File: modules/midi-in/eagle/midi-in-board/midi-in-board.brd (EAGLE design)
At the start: 100 x 80 mm, 83 parts, among them IC1 LM358N, IC2 TL072P, IC3 TL074P, IC4 TL074P, T1 BC547, T2 BC547, T3 BC547, X1 MIDI IN, X2 MIDI THRU, X3 CHANNEL SELECT SW, X4 POWER IN

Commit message: Start PCB design for main MIDI in board
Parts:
- removed C7: 100n, rcl:C050-024X044
- removed JP5, JP6: (no value), pinhead:1X02
- removed R52, R53: 220R, rcl:0207/7
- removed T3: BC547, transistor:TO92
- removed V1, V2: 74595N, 74ttl-din:DIL16
- JP1: device pinhead:1X08 -> pinhead:1_05X2MM
- JP2: device pinhead:1X08 -> pinhead:1X02
- JP3: device pinhead:1X01 -> pinhead:1X02
- R1: value 220R -> 1K
- R11: value 1K -> 10K
- R15, R49: value 10K -> 1K; device rcl:0207/7 -> pot:CA6V
- R18, R20, R24, R26, R27: value 10K -> 100K
- R2, R5, R50: value 10K -> 220R
- R28, R29, R30, R31, R32: value 100K -> 10K
- R34, R36, R38: value 3.6K -> 10K
- R4: value 220R -> 10K
- R41: value 10K -> 3.6K
- R43, R44: value 1K -> 3.6K; device pot:CA6V -> rcl:0207/7
- R48: value 20K -> 1K; device rcl:0207/7 -> pot:CA6V
- R51: value 1K -> 220R; device pot:CA6V -> rcl:0207/7
- R6: value 10K -> 20K
- X1: value MIDI IN -> POWER IN; device con-molex:22-23-2021 -> con-wago-500:W237-103
- X2: value MIDI THRU -> MIDI IN; device con-molex:22-23-2031 -> con-molex:22-23-2021
- X3: value CHANNEL SELECT SW -> MIDI THRU; device con-molex:22-23-2021 -> con-molex:22-23-2031
- X4: value POWER IN -> CHANNEL SELECT SW; device con-wago-500:W237-103 -> con-molex:22-23-2021
- moved R1 132.3 mm to (90.2, 55.9), turned to 90 degrees
- moved SV2 131.2 mm to (69.8, 54.6)
- moved X4 119.5 mm to (95.2, 53.3), turned to 90 degrees
- moved X1 116.6 mm to (52.1, 11.4)
- moved R4 106.7 mm to (33.0, 47.0), turned to 90 degrees
- moved SV1 101.4 mm to (69.8, 66.0)
- moved R51 100.6 mm to (-27.9, 95.2)
- moved R5 100.0 mm to (12.7, 33.0), turned to 270 degrees
- moved IC1 95.3 mm to (24.1, 31.8), turned to 90 degrees
- moved R44 86.0 mm to (-58.4, 90.2)
- moved R49 84.8 mm to (-66.0, 6.35)
- moved R48 84.6 mm to (-57.1, 6.35)
- moved R43 84.2 mm to (-38.1, 90.2)
- moved R15 83.1 mm to (-74.9, 6.35)
- moved R2 76.1 mm to (16.5, 30.5), turned to 270 degrees
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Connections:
- removed net +UB: V1.16, V2.16
- removed net -UB: V1.8, V2.8
- removed net N$1 (its old number): R1.1, X1.1
- removed net N$25: V1.9, V2.14
- removed net N$30: C2.2, R10.2, V1.10, V2.10
- removed net N$48: JP1.1, V1.15
- removed net N$49: JP1.2, V1.1
- removed net N$50: JP1.3, V1.2
- removed net N$51: JP1.4, V1.3
- removed net N$52: JP1.5, V1.4
- removed net N$54: JP1.6, V1.5
- removed net N$55: JP1.7, V1.6
- removed net N$58: JP1.8, V1.7
- removed net N$60: JP2.1, V2.15
- removed net N$64 (its old number): R38.2, R45.E
- removed net N$72: JP2.2, V2.1
- removed net N$73: JP2.3, V2.2
- removed net N$74: JP2.4, V2.3
- removed net N$75: JP2.5, V2.4
- removed net N$76: JP2.6, V2.5
- removed net N$77: JP2.7, V2.6
- removed net N$78: JP2.8, V2.7
- removed net N$8: R9.1, T3.2
- removed net V-: C1.1, C2.1, IC1.8, OK1.8, R11.2, R2.2, R3.2, R9.2, SV1.4, T1.3, T2.3, T3.3
- new net N$6: R2.1, X3.1
- new net N$66: R44.2, R49.E
- net GND: now also C2.2, JP1.1, JP2.2, JP3.2, R10.2, R11.2, R14.1, R16.1, R28.1, R8.2, R9.2, X1.2; no longer C7.2, JP5.2, JP6.2, R10.1, R13.2, R14.2, R15.2, R16.2, R50.1, R6.1, R8.1, T3.1, V1.13, V2.13, X2.2
- net N$10: now also R32.2, R33.2, R38.1; no longer R24.2, R26.2, R39.1
- net N$11: now also R7.1; no longer R5.1
- net N$12: now also R22.1; no longer R7.1
- net N$13: now also C2.1, R8.1; no longer C3.1, R12.1
- net N$14: now also R1.1, X4.1; no longer R11.1, X3.1
- net N$15: now also C3.1, R18.1, R9.1; no longer C4.1, R13.1, R19.1
- net N$16: now also C4.1, R10.1, R19.1; no longer C5.1, R14.1, R21.1
- net N$17: now also C5.1, R11.1, R20.1; no longer C6.1, R15.1, R23.1
- net N$18: now also C6.1, R12.1, R21.1; no longer C7.1, R16.1, R25.1
- net N$19: now also R7.2; no longer R5.2
- net N$2: now also R3.2; no longer R1.2
- net N$20: now also R16.2, R50.1; no longer R52.1, R6.2
- net N$21: now also R22.2; no longer R7.2
- net N$22: now also R28.2, R51.1; no longer R53.1, R8.2
- net N$23: now also R26.2, R32.1, R33.1; no longer R24.1, R26.1, R31.2
- net N$24: now also JP1.4; no longer V1.11, V2.11
- net N$26: now also JP1.3; no longer V1.12, V2.12
- net N$27: now also R23.1; no longer R28.1
- net N$28: now also R18.2, R24.1; no longer R19.2, R29.1
- net N$29: now also R19.2, R25.1; no longer R21.2, R30.1
- net N$3: now also X2.2; no longer X1.2
- net N$31: now also R20.2, R26.1; no longer R23.2, R31.1
- net N$32: now also R21.2, R27.1; no longer R25.2, R32.1
- net N$33: now also R23.2, R29.1; no longer R18.1, R28.2
- net N$34: now also R29.2, R35.1; no longer R18.2, R33.1
- net N$35: now also R24.2, R30.1; no longer R20.1, R29.2
- net N$36: now also R30.2, R36.1; no longer R20.2, R35.1
- net N$37: now also R25.2, R31.1; no longer R22.1, R30.2
- net N$38: now also R31.2; no longer R22.2
- net N$39: now also R27.2, R34.1; no longer R27.1, R32.2
- net N$4: now also R5.1; no longer R4.1
- net N$40: now also R34.2, R39.1; no longer R27.2, R41.1
- net N$41: now also X1.3; no longer X4.3
- net N$42: now also R14.2, R15.A; no longer R50.2, R51.A
- net N$44: now also R13.2, R6.1; no longer R48.1, R49.2
- net N$45: now also R13.1, R15.E; no longer R49.1, R51.E
- net N$46: now also R15.S; no longer R51.S
- net N$5: now also R4.1; no longer R2.1
- net N$53: now also R35.2, R40.1; no longer R33.2, R34.1
- net N$56: now also R36.2, R41.1; no longer R35.2, R36.1
- net N$57: now also R42.1; no longer R38.1
- net N$59: now also R38.2, R43.1; no longer R39.2, R40.1
- net N$61: now also R39.2, R44.1; no longer R41.2, R42.1
- net N$62: now also R40.2, R45.E; no longer R34.2, R43.E
- net N$63: now also R41.2, R46.E; no longer R36.2, R44.E
- net N$65: now also R43.2, R48.E; no longer R40.2, R46.E
- net N$67: now also R45.A; no longer R43.A
- net N$68: now also R46.A; no longer R44.A
- net N$69: now also R47.A; no longer R45.A
- net N$7: now also R5.2, X3.3; no longer R4.2, X2.3
- net N$70: now also R48.A; no longer R46.A
- net N$71: now also R49.A; no longer R47.A
- net N$79: now also JP2.1, R50.2; no longer JP5.1, R52.2
- net N$80: now also JP3.1, R51.2; no longer JP6.1, R53.2
- net N$9: now also JP1.5; no longer V1.14
- net VCC: now also C1.1, IC1.8, JP1.2, OK1.8, R1.2, R2.2, R4.2, R6.2, SV1.4, T1.3, T2.3, X1.1; no longer JP3.1, R48.2, X4.1
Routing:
- net VCC: track 0.00 -> 169.7 mm
- net N$5: track 0.00 -> 58.8 mm
- net N$14: track 0.00 -> 35.1 mm
- net N$4: track 0.00 -> 31.6 mm
- net N$3: track 0.00 -> 14.3 mm
- net N$6: track 0.00 -> 11.0 mm
- net N$2: track 0.00 -> 8.67 mm
- net N$7: track 0.00 -> 5.08 mm
- net N$1: track 0.00 -> 4.86 mm
- added copper zone on layer 16, net GND

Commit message: Progress on MIDI in main board. Nightmare.
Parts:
- removed JP1: (no value), pinhead:1_05X2MM
- added X5: 22-23-2051, con-molex:22-23-2051
- moved T1 165.6 mm to (85.1, 44.5)
- moved R9 165.5 mm to (68.6, 19.1), turned to 90 degrees
- moved JP3 161.0 mm to (95.2, 31.8), turned to 270 degrees
- moved IC2 160.0 mm to (76.2, 30.5), turned to 270 degrees
- moved R7 157.4 mm to (73.7, 44.5), turned to 270 degrees
- moved JP2 153.3 mm to (95.2, 41.9), turned to 270 degrees
- moved R8 151.0 mm to (68.6, 36.8), turned to 270 degrees
- moved R40 150.5 mm to (76.2, 17.8)
- moved R19 149.4 mm to (55.9, 38.1), turned to 270 degrees
- moved JP4 145.9 mm to (95.2, 16.5), turned to 270 degrees
- moved R29 144.3 mm to (76.2, 22.9)
- moved R18 143.4 mm to (63.5, 19.1), turned to 90 degrees
- moved R35 140.3 mm to (76.2, 20.3), turned to 180 degrees
- moved IC3 136.0 mm to (52.1, 26.7)
- moved R28 133.0 mm to (88.9, 30.5), turned to 180 degrees
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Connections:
- removed net GND: C1.2, C2.2, C3.2, C4.2, C5.2, C6.2, IC1.4, IC2.5, IC3.12, IC3.5, IC4.12, IC4.5, JP1.1, JP2.2, JP3.2, OK1.5, R10.2, R11.2, R12.2, R14.1, R16.1, R28.1, R8.2, R9.2, SV1.2, X1.2, X3.2, X4.2
- removed net N$43: IC4.11
- new net N$8: C1.2, C2.2, C3.2, C4.2, C5.2, C6.2, IC1.4, IC2.5, IC3.12, IC3.5, IC4.12, IC4.5, JP2.2, JP3.2, OK1.5, R10.2, R11.2, R12.2, R14.1, R16.1, R28.1, R8.2, R9.2, SV1.2, X1.2, X3.2, X4.2, X5.1
- net N$24: now also X5.4; no longer JP1.4
- net N$26: now also X5.3; no longer JP1.3
- net N$41: now also IC4.11
- net N$9: now also X5.5; no longer JP1.5
- net VCC: now also X5.2; no longer JP1.2
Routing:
- net VCC: track 169.7 -> 290.9 mm
- net N$24: track 0.00 -> 58.0 mm
- net N$67: track 0.00 -> 43.6 mm
- net N$9: track 0.00 -> 40.8 mm
- net N$20: track 0.00 -> 33.4 mm
- net N$26: track 0.00 -> 32.4 mm
- net N$13: track 0.00 -> 25.3 mm
- net N$22: track 0.00 -> 25.1 mm
- net N$28: track 0.00 -> 20.1 mm
- net N$16: track 0.00 -> 19.4 mm
- net N$34: track 0.00 -> 18.4 mm
- net N$21: track 0.00 -> 16.6 mm
- net N$19: track 0.00 -> 15.3 mm
- net N$33: track 0.00 -> 14.3 mm
- net N$8: track 0.00 -> 12.5 mm, vias 0 -> 2
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- added copper zone on layer 16, net N$8
- removed copper zone on layer 16, net GND
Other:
- board size 100 x 80 mm -> 102.5 x 83.8 mm

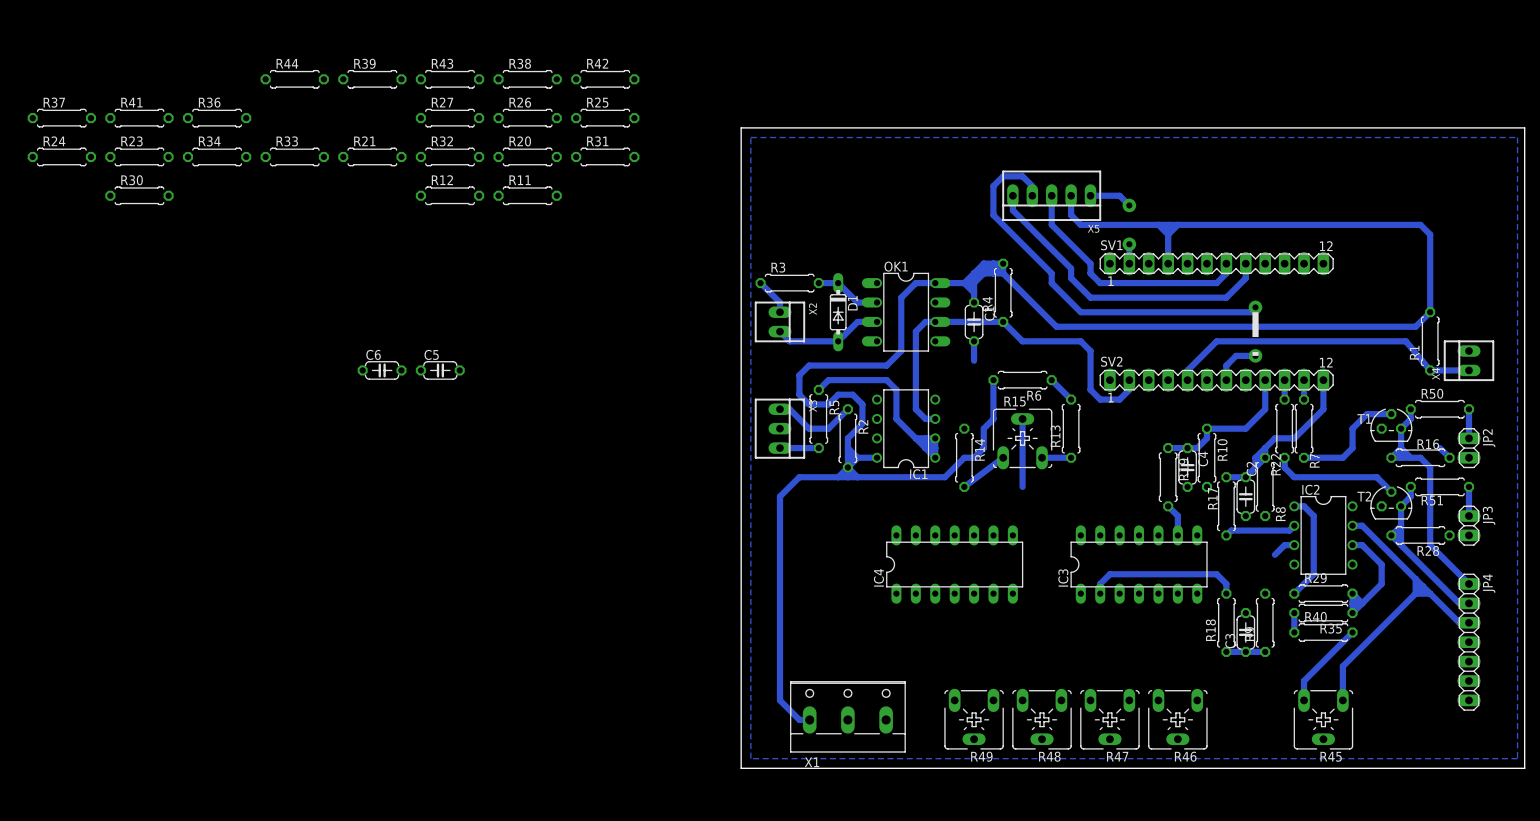
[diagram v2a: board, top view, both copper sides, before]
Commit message: Separate out CV scaling to its own board, finish MIDI in board layout
Non-nightmare!
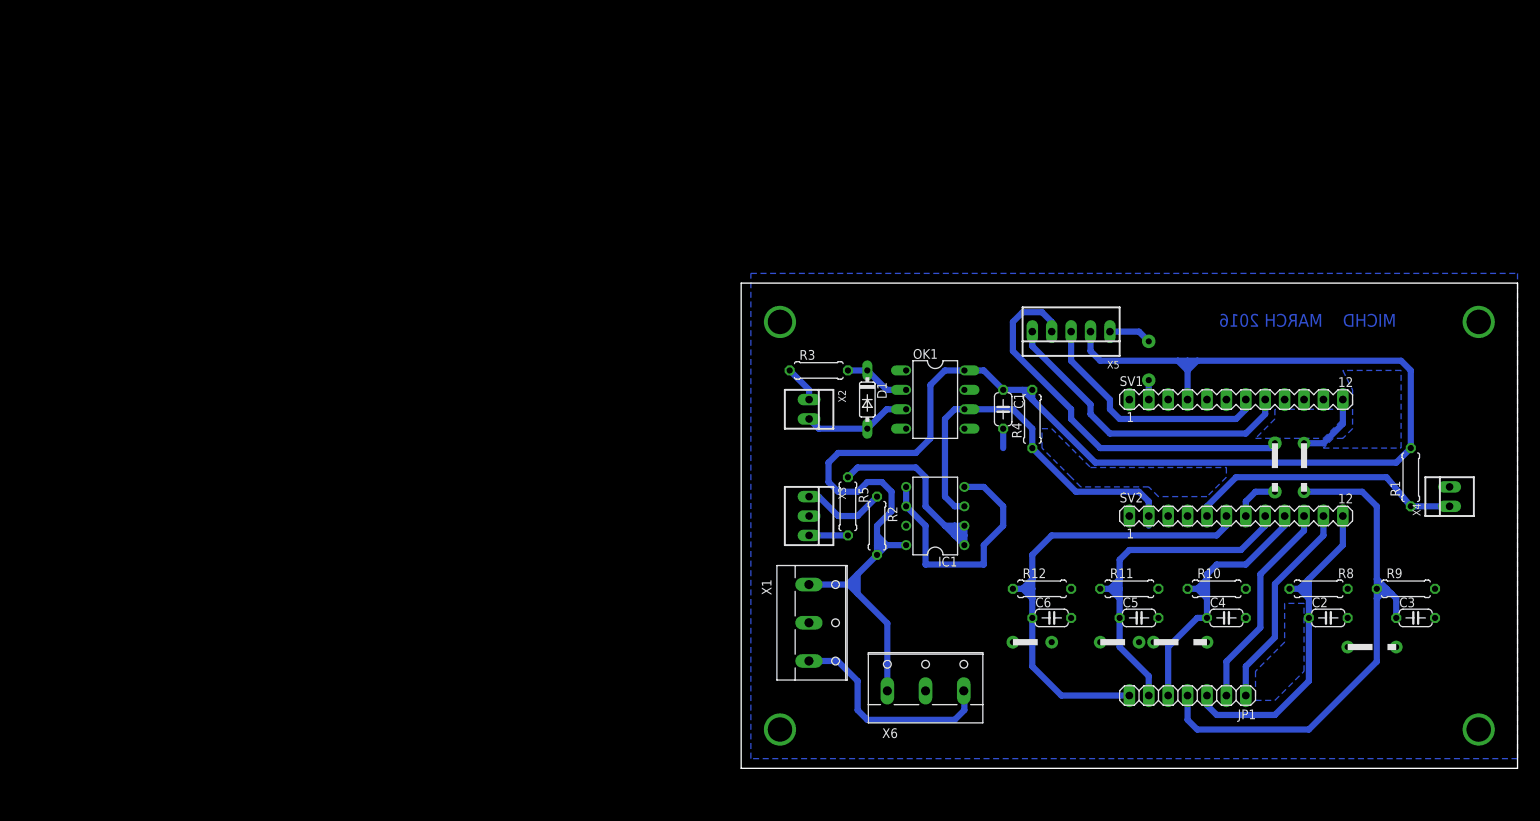
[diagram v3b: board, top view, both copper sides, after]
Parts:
- removed IC2: TL072P, linear:DIL08
- removed IC3, IC4: TL074P, linear:DIL14
- removed JP2, JP3: (no value), pinhead:1X02
- removed JP4: (no value), pinhead:1X07
- removed R13, R14, R16, R22, R28, R29, R30, R31, R32, R33, R34, R35, R36, R37, R38, R39, R7: 10K, rcl:0207/7
- removed R15, R45, R46, R47, R48, R49: 1K, pot:CA6V
- removed R17, R18, R19, R20, R21, R23, R24, R25, R26, R27: 100K, rcl:0207/7
- removed R40, R41, R42, R43, R44: 3.6K, rcl:0207/7
- removed R50, R51: 220R, rcl:0207/7
- removed R6: 20K, rcl:0207/7
- removed T1, T2: BC547, transistor:TO92
- added JP1: (no value), pinhead:1X07
- added X6: POWER OUT CV, con-wago-500:W237-103
- moved C5 97.0 mm to (52.1, 19.7)
- moved R11 94.1 mm to (50.8, 23.5)
- moved C6 93.4 mm to (40.6, 19.7)
- moved R12 93.0 mm to (39.4, 23.5)
- moved C3 22.3 mm to (88.3, 19.7), turned to 0 degrees
- moved C4 20.3 mm to (63.5, 19.7), turned to 0 degrees
- moved C2 19.2 mm to (76.8, 19.7), turned to 0 degrees
- moved R9 18.9 mm to (87.0, 23.5), turned to 0 degrees
- moved SV1 18.0 mm to (64.8, 48.3)
- moved X5 18.0 mm to (43.2, 57.1)
- moved R1 18.0 mm to (87.6, 38.1)
- moved X4 18.0 mm to (92.7, 35.6)
- moved SV2 18.0 mm to (64.8, 33.0)
- moved R10 17.2 mm to (62.2, 23.5), turned to 0 degrees
- moved R4 16.9 mm to (38.1, 45.7)
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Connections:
- removed net N$15: C3.1, R18.1, R9.1, SV1.12
- removed net N$19: R7.2, T1.2
- removed net N$21: R22.2, T2.2
- removed net N$22: JP4.2, R28.2, R51.1, T2.1
- removed net N$23: IC4.1, R26.2, R32.1, R33.1
- removed net N$27: IC2.2, R17.2, R23.1
- removed net N$28: IC3.2, R18.2, R24.1
- removed net N$29: IC3.9, R19.2, R25.1
- removed net N$31: IC4.2, R20.2, R26.1
- removed net N$32: IC4.9, R21.2, R27.1
- removed net N$33: IC2.1, R23.2, R29.1
- removed net N$34: IC2.6, R29.2, R35.1
- removed net N$35: IC3.1, R24.2, R30.1
- removed net N$36: IC3.6, R30.2, R36.1
- removed net N$37: IC3.8, R25.2, R31.1
- removed net N$38: IC3.13, R31.2, R37.1
- removed net N$39: IC4.8, R27.2, R34.1
- removed net N$40: IC4.13, R34.2, R39.1
- removed net N$41: IC2.4, IC3.11, IC4.11, X1.3
- removed net N$42: R14.2, R15.A
- removed net N$44: R13.2, R6.1
- removed net N$45: R13.1, R15.E
- removed net N$46: IC2.3, IC3.10, IC3.3, IC4.10, IC4.3, R15.S
- removed net N$53: R35.2, R40.1
- removed net N$56: R36.2, R41.1
- removed net N$57: R37.2, R42.1
- removed net N$59: R38.2, R43.1
- removed net N$61: R39.2, R44.1
- removed net N$62: R40.2, R45.E
- removed net N$63: R41.2, R46.E
- removed net N$64: R42.2, R47.E
- removed net N$65: R43.2, R48.E
- removed net N$66: R44.2, R49.E
- removed net N$67: IC2.7, JP4.3, R45.A
- removed net N$68: IC3.7, JP4.4, R46.A
- removed net N$69: IC3.14, JP4.5, R47.A
- removed net N$70: IC4.7, JP4.6, R48.A
- removed net N$71: IC4.14, JP4.7, R49.A
- removed net N$79: JP2.1, R50.2
- removed net N$8: C1.2, C2.2, C3.2, C4.2, C5.2, C6.2, IC1.4, IC2.5, IC3.12, IC3.5, IC4.12, IC4.5, JP2.2, JP3.2, OK1.5, R10.2, R11.2, R12.2, R14.1, R16.1, R28.1, R8.2, R9.2, SV1.2, X1.2, X3.2, X4.2, X5.1
- removed net N$80: JP3.1, R51.2
- new net GND: C1.2, C2.2, C3.2, C4.2, C5.2, C6.2, IC1.4, IC1.5, IC1.6, OK1.5, R10.2, R11.2, R12.2, R8.2, R9.2, SV1.2, X1.2, X3.2, X4.2, X5.1, X6.2
- net N$10: now also X1.3, X6.3; no longer IC4.6, R32.2, R33.2, R38.1
- net N$11: now also JP1.1; no longer R7.1
- net N$12: now also JP1.2; no longer R22.1
- net N$13: now also JP1.3; no longer R17.1
- net N$16: now also JP1.5; no longer R19.1
- net N$17: now also JP1.6; no longer R20.1
- net N$18: now also JP1.7; no longer R21.1
- net N$20: now also C3.1, JP1.4, R9.1, SV1.12; no longer JP4.1, R16.2, R50.1, T1.1
- net VCC: now also X6.1; no longer IC2.8, IC3.4, IC4.4, R6.2, T1.3, T2.3
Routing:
- net VCC: track 290.9 -> 217.2 mm
- net N$18: track 0.00 -> 63.3 mm
- net N$20: track 33.4 -> 82.6 mm, vias 0 -> 2
- net N$17: track 0.00 -> 47.7 mm
- net GND: track 0.00 -> 44.3 mm, vias 0 -> 10
- net N$67: track 43.6 -> 0.00 mm
- net N$10: track 0.00 -> 28.8 mm
- net N$12: track 2.54 -> 27.7 mm
- net N$11: track 2.54 -> 27.7 mm
- net N$22: track 25.1 -> 0.00 mm
- net N$13: track 25.3 -> 46.5 mm
- net N$16: track 19.4 -> 40.2 mm
- net N$28: track 20.1 -> 0.00 mm
- net N$34: track 18.4 -> 0.00 mm
- net N$21: track 16.6 -> 0.00 mm
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- added copper zone on layer 16, net GND
- added copper zone on layer 16, net N$15
- added copper zone on layer 16, net N$19
- added copper zone on layer 16, net N$21
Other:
- board size 102.5 x 83.8 mm -> 101.6 x 63.5 mm
- board text added: "MICHD MARCH 2016"
